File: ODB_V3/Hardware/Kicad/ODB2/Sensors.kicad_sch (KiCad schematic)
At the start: 20 parts, among them J4 RF2-04A-T-00-50-G, U2 LMT70YFQT, U4 MS580301BA01-00, U5 L76L-M33, U6 BNO055

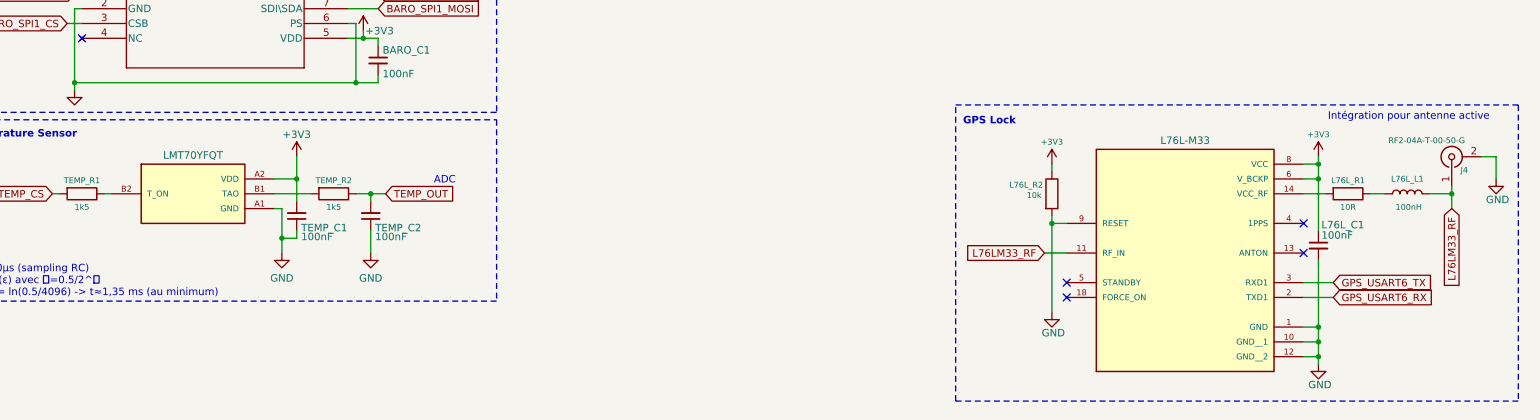
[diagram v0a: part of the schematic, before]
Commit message: fix: swipe filter breakoutboard VCC to main connector side
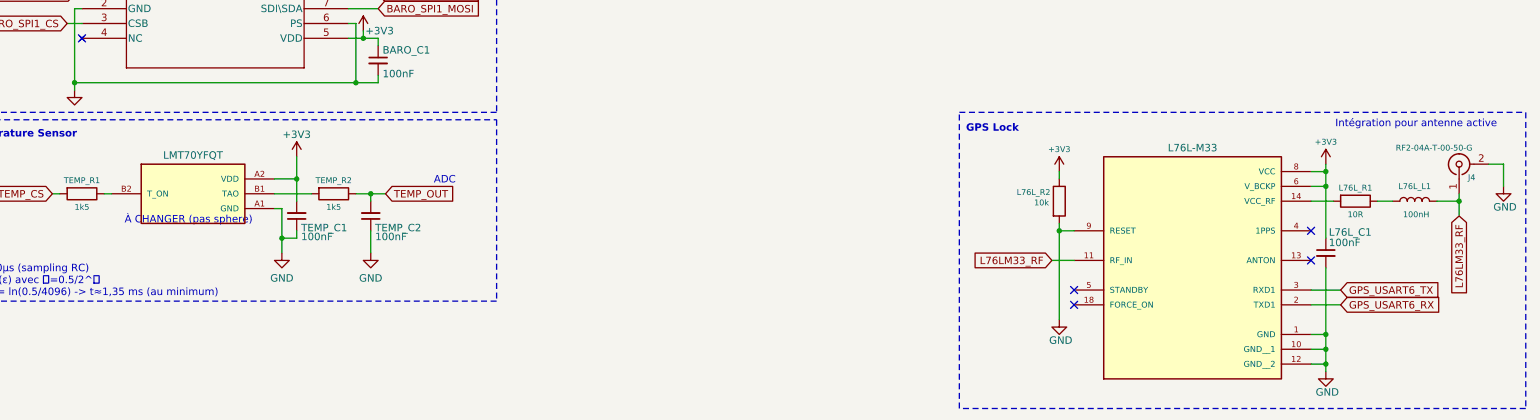
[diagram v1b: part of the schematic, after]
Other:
- note added: "À CHANGER (pas sphere)"
- moved on the sheet: J4, L76L_C1, L76L_L1, L76L_R1, L76L_R2

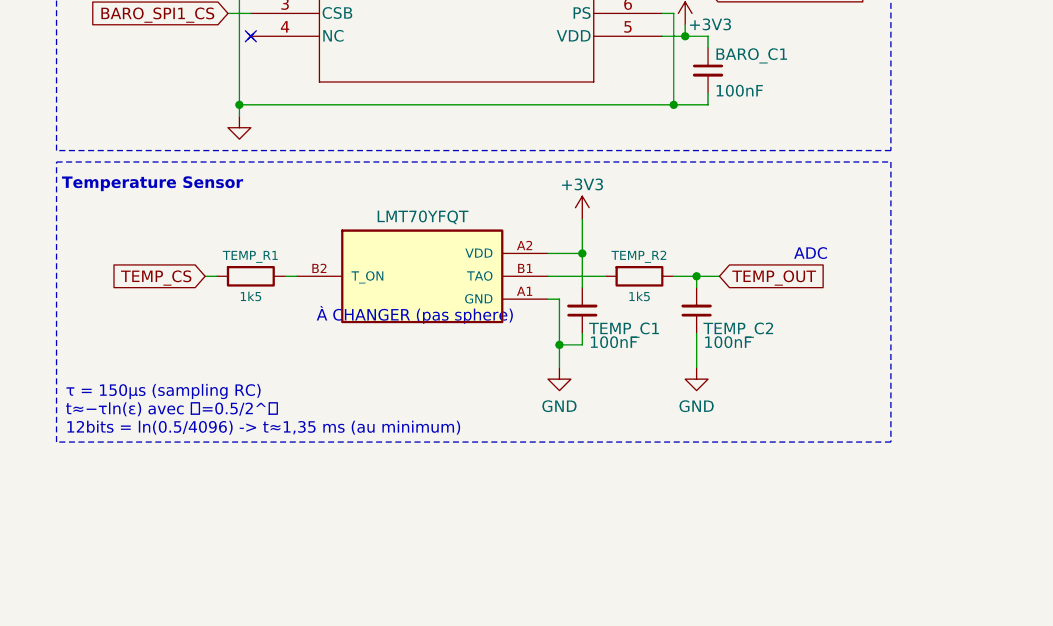
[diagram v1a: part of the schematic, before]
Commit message: fix: change temperature sensor, readd footprint pyros and powersupply components,
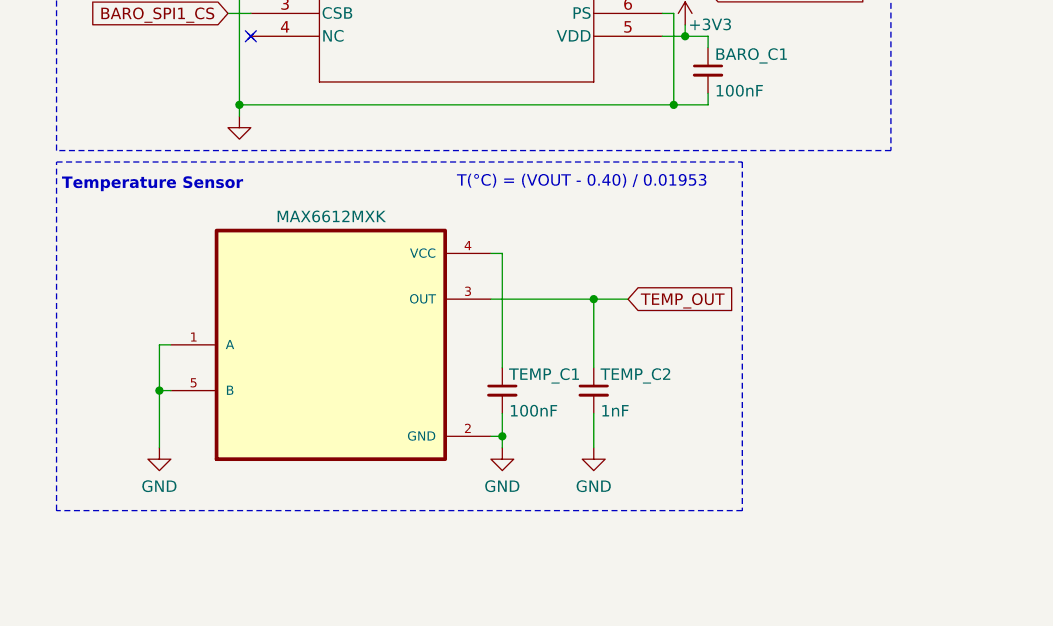
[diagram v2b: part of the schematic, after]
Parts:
- removed TEMP_R1, TEMP_R2: 1k5, Resistor_SMD:R_0603_1608Metric, symbol Device:R
- removed U2: LMT70YFQT, LMT70YFQT:BGA4C40P2X2_88X88X68, symbol ODB2:LMT70YFQT
- added U9: MAX6612MXK, MAX6612MXK:SOT65P210X110-5N, symbol ODB2:MAX6612MXK
- TEMP_C2: value 100nF -> 1nF
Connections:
- net +3V3: no longer TEMP_C1.2
- net GND: now also TEMP_C1.2, TEMP_C2.2, U9.1 (A), U9.2 (GND), U9.5 (B); no longer TEMP_C1.1, TEMP_C2.1
- net TEMP_OUT: now also TEMP_C2.1, U9.3 (OUT); no longer TEMP_C2.2
- new net: TEMP_C1.1, U9.4 (VCC)
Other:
- note added: "T(°C) = (VOUT - 0.40) / 0.01953"
- note removed: "ADC"
- note removed: "À CHANGER (pas sphere)"
- note removed: "τ = 150µs (sampling RC) t≈−τln(ε) avec 𝜀=0.5/2^𝑁 12bits = ln(0.5/4096) -> t≈1,35 ms (au minimum)"

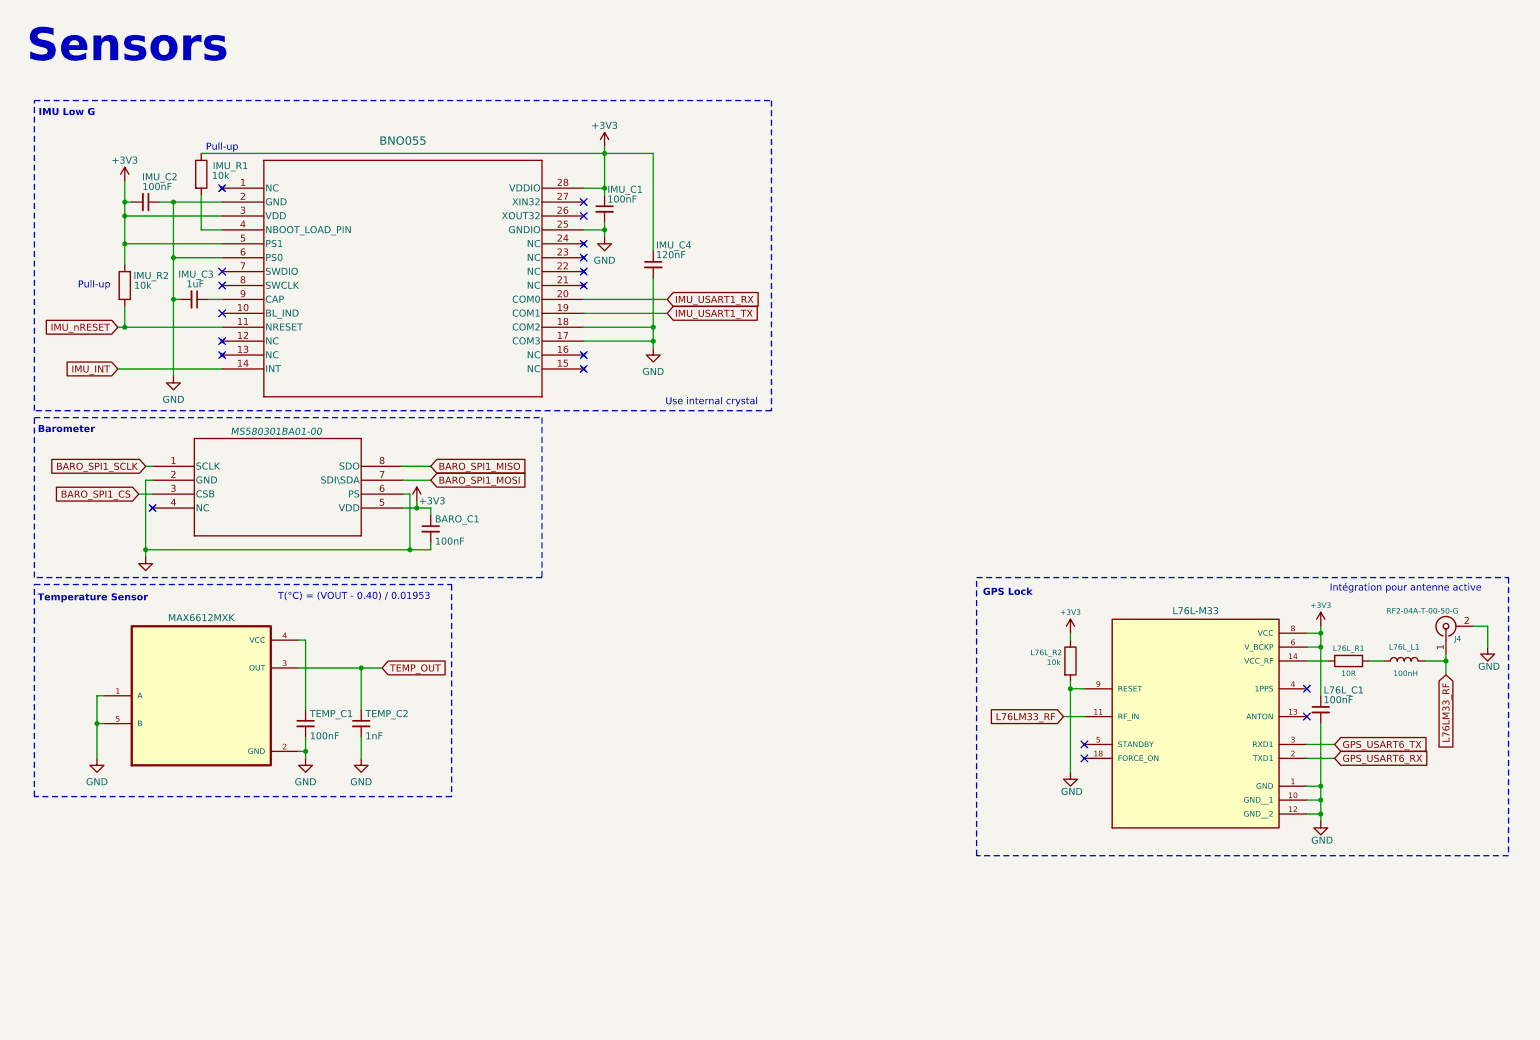
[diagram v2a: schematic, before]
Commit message: feat: add acceleromter high g, fix communication protocole mapping excel, fix beacon i2c connector (id i2c channel) and add footprint/symbole accelerometer
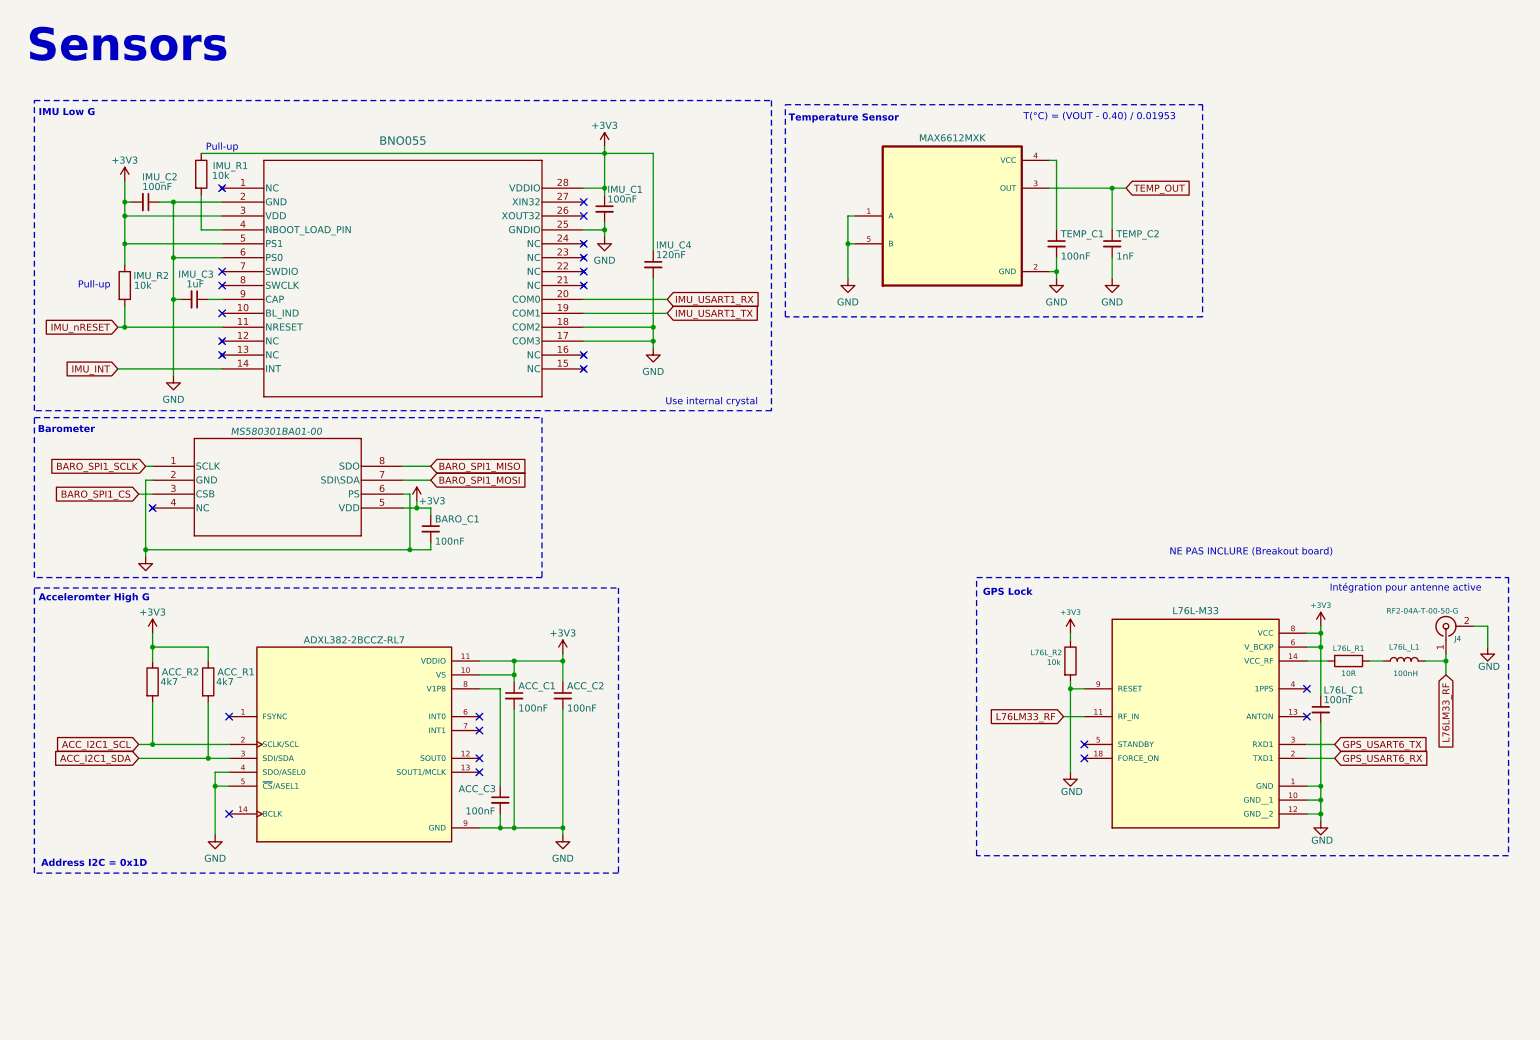
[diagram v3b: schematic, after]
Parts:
- added ACC_C1, ACC_C2, ACC_C3: 100nF, Capacitor_SMD:C_0603_1608Metric, symbol Device:C_Small
- added ACC_R1, ACC_R2: 4k7, Resistor_SMD:R_0603_1608Metric, symbol Device:R
- added U10: ADXL382-2BCCZ-RL7, ADXL382-2BCCZ-RL7:XDCR_ADXL382-2BCCZ-RL7, symbol ODB2:ADXL382-2BCCZ-RL7
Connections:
- net +3V3: now also ACC_C1.1, ACC_C2.1, ACC_R1.1, ACC_R2.1, U10.10 (VS), U10.11 (VDDIO)
- net GND: now also ACC_C1.2, ACC_C2.2, ACC_C3.2, U10.4 (SDO/ASEL0), U10.5 (~{CS}/ASEL1), U10.9 (GND)
- new net: ACC_C3.1, U10.8 (V1P8)
- new net ACC_I2C1_SCL: ACC_R2.2, U10.2 (SCLK/SCL)
- new net ACC_I2C1_SDA: ACC_R1.2, U10.3 (SDI/SDA)
- no-connect marks 19 -> 25
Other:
- note added: "Acceleromter High G"
- note added: "Address I2C = 0x1D"
- note added: "NE PAS INCLURE (Breakout board)"
- moved on the sheet: TEMP_C1, TEMP_C2

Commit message: repo: New PSU design
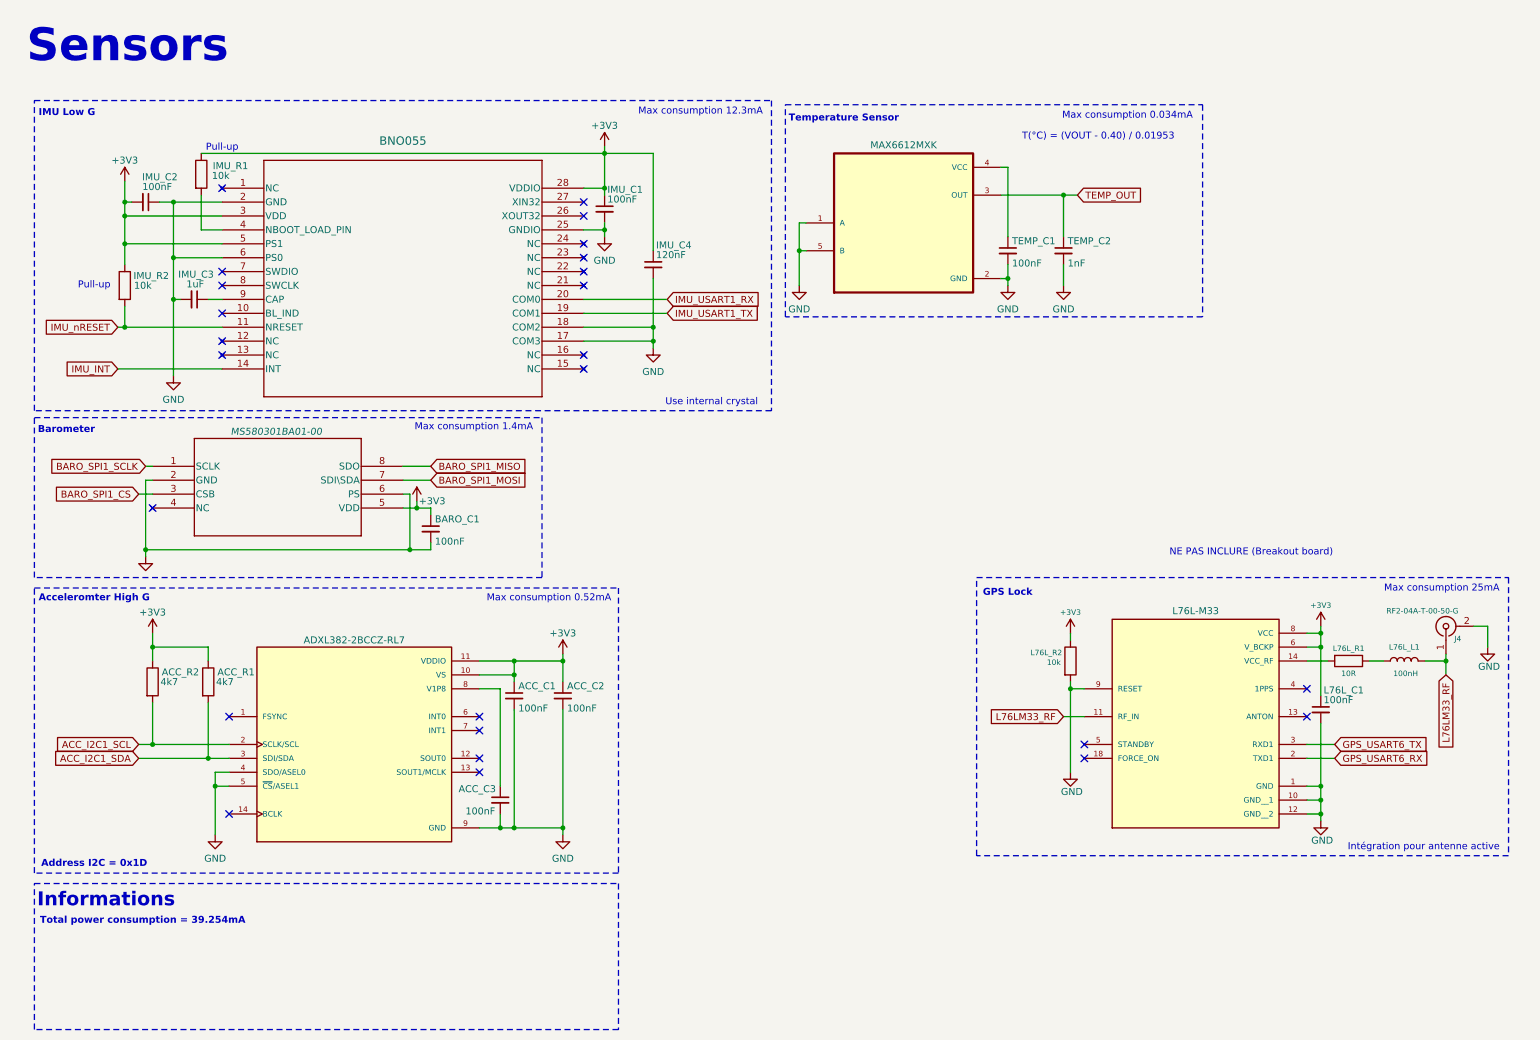
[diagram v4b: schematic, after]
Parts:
- J4, L76L_C1, L76L_L1, L76L_R1, L76L_R2, U5: now left out of the parts list
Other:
- note added: "Informations"
- note added: "Max consumption 0.034mA"
- note added: "Max consumption 0.52mA"
- note added: "Max consumption 1.4mA"
- note added: "Max consumption 12.3mA"
- note added: "Max consumption 25mA"
- note added: "Total power consumption = 39.254mA"
- moved on the sheet: TEMP_C1, TEMP_C2

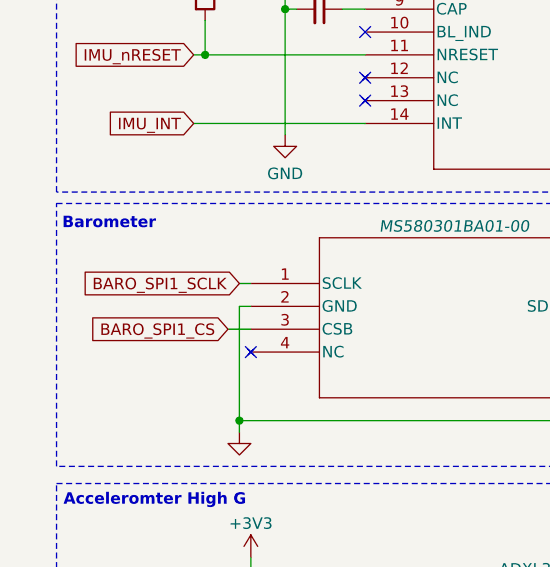
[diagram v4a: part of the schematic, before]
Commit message: feat: add kicad pinout (missing), rename BARO_SPI1_SCLK->CLK
Missing Pinout:
IMU_INT
TEMP_OUT
GPS_FUNCT_X
BUZ_PWM
VIN_An
Senses_X
Fire_X
Pyro_Arm
PA_An
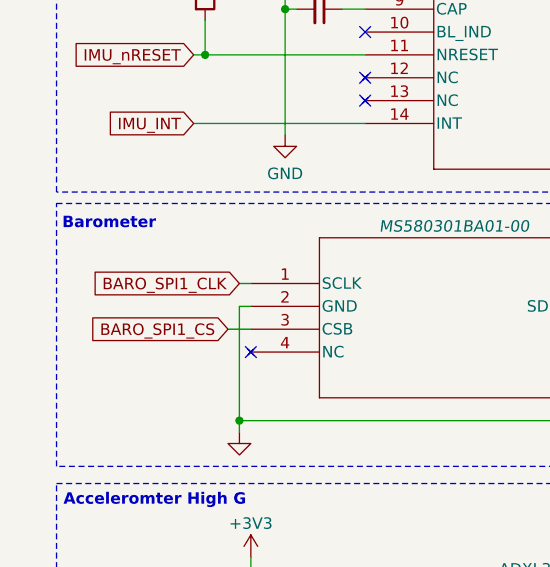
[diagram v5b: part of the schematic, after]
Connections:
- net BARO_SPI1_SCLK renamed BARO_SPI1_CLK
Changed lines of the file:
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@@
 		)
 	)
-	(global_label "BARO_SPI1_SCLK"
+	(global_label "BARO_SPI1_CLK"
 		(shape input)
 		(at 34.29 93.98 180)
@@
 		)
 		(property "Intersheetrefs" "${INTERSHEET_REFS}"
-			(at 15.3391 93.98 0)
+			(at 16.5486 93.98 0)
 			(effects
 				(font

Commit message: fx: fixes and add VERIFIER
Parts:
- J4, L76L_C1, L76L_L1, L76L_R1, L76L_R2, U5: now in the parts list
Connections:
- net +3V3: now also TEMP_C1.1, U9.4 (VCC)
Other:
- note added: "1.8 V if VS Grounded"
- note added: "ADC 10bits"
- note added: "Active low"
- note added: "Addess selection 0x1D ASEL0=ASEL1=GND"
- note added: "Digital OUT"
- note added: "LOW=chip select"
- note added: "OSC (optional)"
- note added: "PAS INCLUT SUR LE PCB (Attributs) (Breakout board)"
- note added: "POSSIBLE I2C (VERIFIER)"
- note added: "RX"
- note added: "SÉPARER VDD et VDDIO"
- note added: "T(°C) ≈ (VOUT - 0.40) / 0.01953"
- note added: "TX"
- note added: "VÉRIFIER !!!"
- note removed: "NE PAS INCLURE (Breakout board)"
- note removed: "T(°C) = (VOUT - 0.40) / 0.01953"

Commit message: fix: 1ere meeting fixes
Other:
- note removed: "POSSIBLE I2C (VERIFIER)"
- note removed: "SÉPARER VDD et VDDIO"
- note removed: "VÉRIFIER !!!"
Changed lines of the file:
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@@
-		)
-	)
-	(text "SÉPARER VDD et VDDIO"
-		(exclude_from_sim no)
-		(at 107.188 122.174 0)
-		(effects
-			(font
-				(size 1.27 1.27)
-			)
 		)
 	)
@@
 		)
 	)
-	(text "VÉRIFIER !!!"
-		(exclude_from_sim no)
-		(at 22.098 66.548 0)
-		(effects
-			(font
-				(size 1.27 1.27)
-				(thickness 0.254)
-				(bold yes)
-			)
-		)
-	)
 	(text "Active low"
 		(exclude_from_sim no)
@@
 		(effects
 			(font
-				(size 1.27 1.27)
-			)
-		)
-	)
-	(text "POSSIBLE I2C (VERIFIER)"
-		(exclude_from_sim no)
-		(at 28.956 91.44 0)
-		(effects
-			(font

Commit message: fix: labels
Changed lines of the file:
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@@
 	(rectangle
 		(start 151.13 27.94)
-		(end 227.33 66.675)
+		(end 227.33 67.31)
 		(stroke
 			(width 0)
@@
 	(text "OSC (optional)"
 		(exclude_from_sim no)
-		(at 91.948 46.482 0)
+		(at 90.678 46.736 0)
 		(effects
 			(font
